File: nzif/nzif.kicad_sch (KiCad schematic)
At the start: 14 parts, among them J1 Rx, J10 ADAU1467_GPIOS, J11 ADAU1467_AUX_ADCS, J4 6V, J6 Microcontroller, J7 USBi, J8 I2S2, J9 I2S1

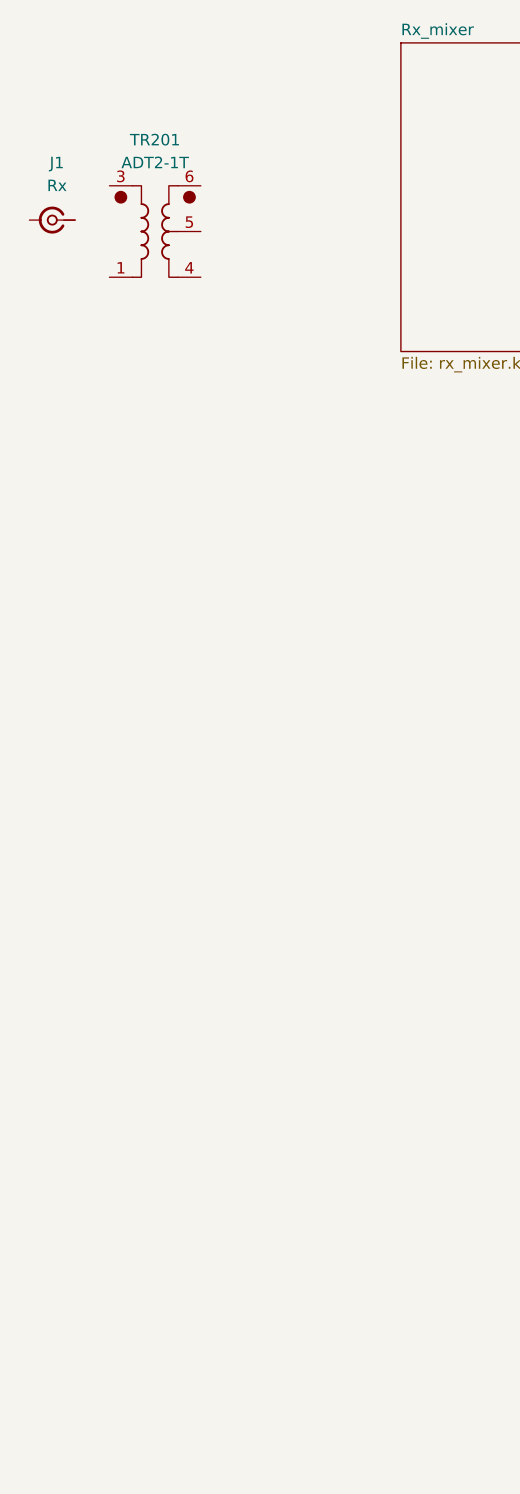
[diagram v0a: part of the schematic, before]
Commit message: changed to 1:1 transformer
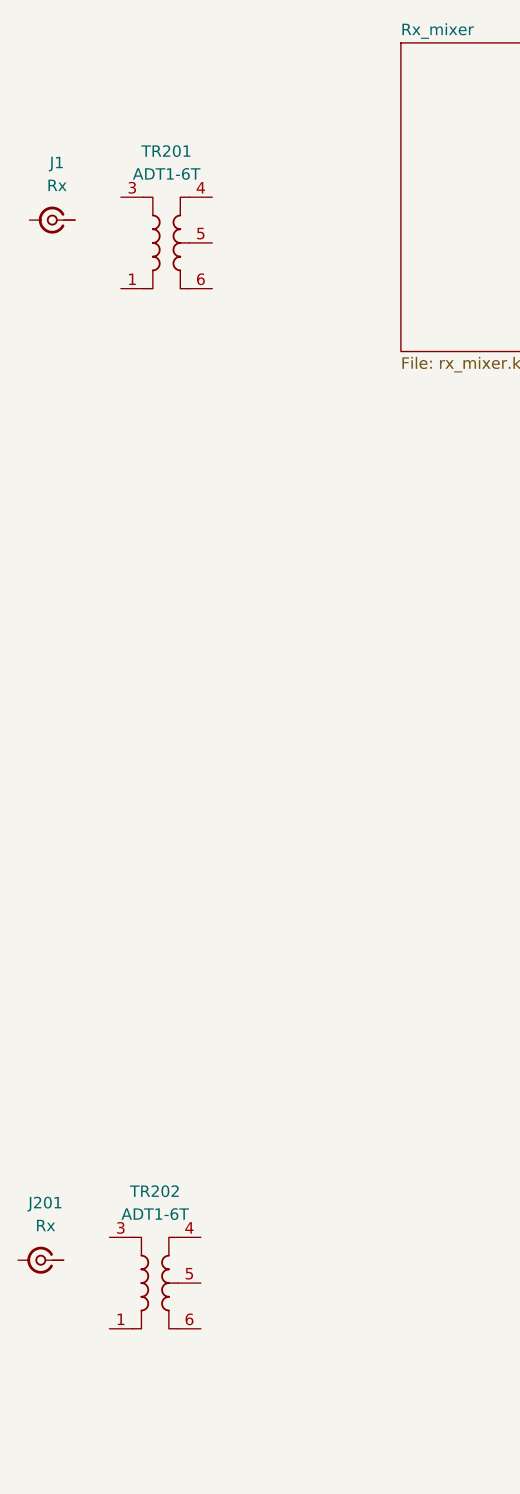
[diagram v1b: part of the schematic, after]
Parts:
- removed TR201: ADT2-1T, RF_Mini-Circuits:Mini-Circuits_CD542_H2.84mm, symbol Transformer:ADT2-1T
- added J201: Rx, symbol Connector:Conn_Coaxial_Small
- added TR201, TR202: ADT1-6T, RF_Mini-Circuits:Mini-Circuits_CD637_H5.23mm, symbol Transformer:ADT1-6T
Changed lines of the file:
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@@
-	)
-	(symbol
-		(lib_id "Transformer:ADT2-1T")
-		(at 41.91 38.1 0)
-		(unit 1)
-		(exclude_from_sim no)
-		(in_bom yes)
-		(on_board yes)
-		(dnp no)
-		(fields_autoplaced yes)
-		(property "Reference" "TR201"
-			(at 41.91 27.94 0)
-			(effects
-				(font
-					(size 1.27 1.27)
-				)
-			)
-		)
-		(property "Value" "ADT2-1T"
-			(at 41.91 30.48 0)
-			(effects
-				(font
-					(size 1.27 1.27)
-				)
-			)
-		)
-		(property "Footprint" "RF_Mini-Circuits:Mini-Circuits_CD542_H2.84mm"
-			(at 41.91 46.99 0)
-			(effects
-				(font
-					(size 1.27 1.27)
-				)
-				(hide yes)
-			)
-		)
-		(property "Datasheet" "https://www.minicircuits.com/pdfs/ADT2-1T+.pdf"
-			(at 41.91 38.1 0)
-			(effects
-				(font
-					(size 1.27 1.27)
-				)
-				(hide yes)
-			)
-		)
-		(property "Description" "0.40-450MHz 1:2 RF Transformer, Unbalanced to Balanced Center Tap, CD542"
-			(at 41.91 38.1 0)
-			(effects
-				(font
-					(size 1.27 1.27)
-				)
-				(hide yes)
-			)
-		)
-		(pin "2"
-		)
-		(pin "6"
-		)
-		(pin "5"
-		)
-		(pin "4"
-		)
-		(pin "3"
-		)
-		(pin "1"
-		)
-		(instances
-			(project ""
-				(path "/fe42ca2f-2bb8-4d5a-9e84-807788ed632f"
-					(reference "TR201")
-					(unit 1)
-				)
-			)
-		)
 	)
 	(symbol
@@
 	)
 	(symbol
+		(lib_id "Transformer:ADT1-6T")
+		(at 41.91 154.94 0)
+		(unit 1)
+		(exclude_from_sim no)
+		(in_bom yes)
+		(on_board yes)
+		(dnp no)
+		(fields_autoplaced yes)
+		(property "Reference" "TR202"
+			(at 41.91 144.78 0)
+			(effects
+				(font
+					(size 1.27 1.27)
+				)
+			)
+		)
+		(property "Value" "ADT1-6T"
+			(at 41.91 147.32 0)
+			(effects
+				(font
+					(size 1.27 1.27)
+				)
+			)
+		)
+		(property "Footprint" "RF_Mini-Circuits:Mini-Circuits_CD637_H5.23mm"
+			(at 41.91 163.83 0)
+			(effects
+				(font
+					(size 1.27 1.27)
+				)
+				(hide yes)
+			)
+		)
+		(property "Datasheet" "https://www.minicircuits.com/pdfs/ADT1-6T+.pdf"
+			(at 41.91 154.94 0)
+			(effects
+				(font
+					(size 1.27 1.27)
+				)
+				(hide yes)
+			)
+		)
+		(property "Description" "0.06-160MHz 1:1 RF Transformer, Unbalanced to Balanced Center Tap, CD542"
+			(at 41.91 154.94 0)
+			(effects
+				(font
+					(size 1.27 1.27)
+				)
+				(hide yes)
+			)
+		)
+		(pin "1"
+		)
+		(pin "5"
+		)
+		(pin "4"
+		)
+		(pin "6"
+		)
+		(pin "3"
+		)
+		(instances
+			(project "nzif"
+				(path "/fe42ca2f-2bb8-4d5a-9e84-807788ed632f"
+					(reference "TR202")
+					(unit 1)
+				)
+			)
+		)
+	)
+	(symbol
 		(lib_id "Device:R_Small_US")
 		(at 398.78 45.72 270)
@@
 	)
 	(symbol
+		(lib_id "Transformer:ADT1-6T")
+		(at 43.18 39.37 0)
+		(unit 1)
+		(exclude_from_sim no)
+		(in_bom yes)
+		(on_board yes)
+		(dnp no)
+		(fields_autoplaced yes)
+		(property "Reference" "TR201"
+			(at 43.18 29.21 0)
+			(effects
+				(font
+					(size 1.27 1.27)
+				)
+			)
+		)
+		(property "Value" "ADT1-6T"
+			(at 43.18 31.75 0)
+			(effects
+				(font
+					(size 1.27 1.27)
+				)
+			)
+		)
+		(property "Footprint" "RF_Mini-Circuits:Mini-Circuits_CD637_H5.23mm"
+			(at 43.18 48.26 0)
+			(effects
+				(font
+					(size 1.27 1.27)
+				)
+				(hide yes)
+			)
+		)
+		(property "Datasheet" "https://www.minicircuits.com/pdfs/ADT1-6T+.pdf"
+			(at 43.18 39.37 0)
+			(effects
+				(font
+					(size 1.27 1.27)
+				)
+				(hide yes)
+			)
+		)
+		(property "Description" "0.06-160MHz 1:1 RF Transformer, Unbalanced to Balanced Center Tap, CD542"
+			(at 43.18 39.37 0)
+			(effects
+				(font
+					(size 1.27 1.27)
+				)
+				(hide yes)
+			)
+		)
+		(pin "1"
+		)
+		(pin "5"
+		)
+		(pin "4"
+		)
+		(pin "6"
+		)
+		(pin "3"
+		)
+		(instances
+			(project ""
+				(path "/fe42ca2f-2bb8-4d5a-9e84-807788ed632f"
+					(reference "TR201")
+					(unit 1)
+				)
+			)
+		)
+	)
+	(symbol
 		(lib_id "Connector_Generic:Conn_02x10_Odd_Even")
 		(at 346.71 78.74 0)
@@
 					(unit 1)
 				)
+			)
+		)
+	)
+	(symbol
+		(lib_id "Connector:Conn_Coaxial_Small")
+		(at 29.21 152.4 180)
+		(unit 1)
+		(exclude_from_sim no)
+		(in_bom yes)
+		(on_board yes)
+		(dnp no)
+		(fields_autoplaced yes)
+		(property "Reference" "J201"
+			(at 29.7295 146.05 0)
+			(effects
+				(font
+					(size 1.27 1.27)
+				)
+			)
+		)
+		(property "Value" "Rx"
+			(at 29.7295 148.59 0)
+			(effects
+				(font
+					(size 1.27 1.27)
+				)
+			)
+		)
+		(property "Footprint" ""
+			(at 29.21 152.4 0)
+			(effects
+				(font
+					(size 1.27 1.27)
+				)
+				(hide yes)
+			)
+		)
+		(property "Datasheet" "~"
+			(at 29.21 152.4 0)
+			(effects
+				(font
+					(size 1.27 1.27)
+				)
+				(hide yes)
+			)
+		)
+		(property "Description" "small coaxial connector (BNC, SMA, SMB, SMC, Cinch/RCA, LEMO, ...)"
+			(at 29.21 152.4 0)
+			(effects
+				(font
+					(size 1.27 1.27)
+				)
+				(hide yes)
+			)
+		)
+		(pin "2"
+		)
+		(pin "1"
+		)
+		(instances
+			(project "nzif"
+				(path "/fe42ca2f-2bb8-4d5a-9e84-807788ed632f"
+					(reference "J201")
+					(unit 1)
+				)

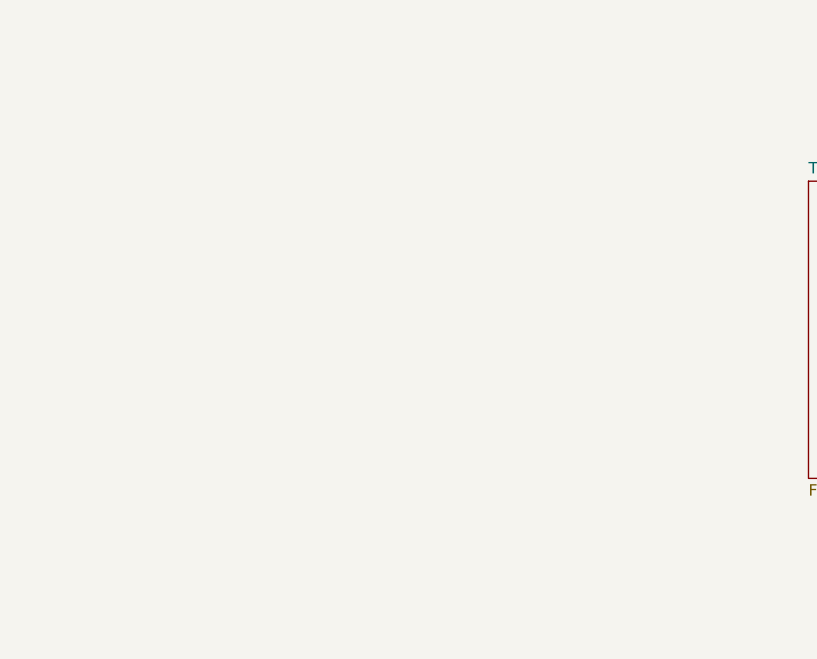
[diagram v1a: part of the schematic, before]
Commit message: added Tx Mixer
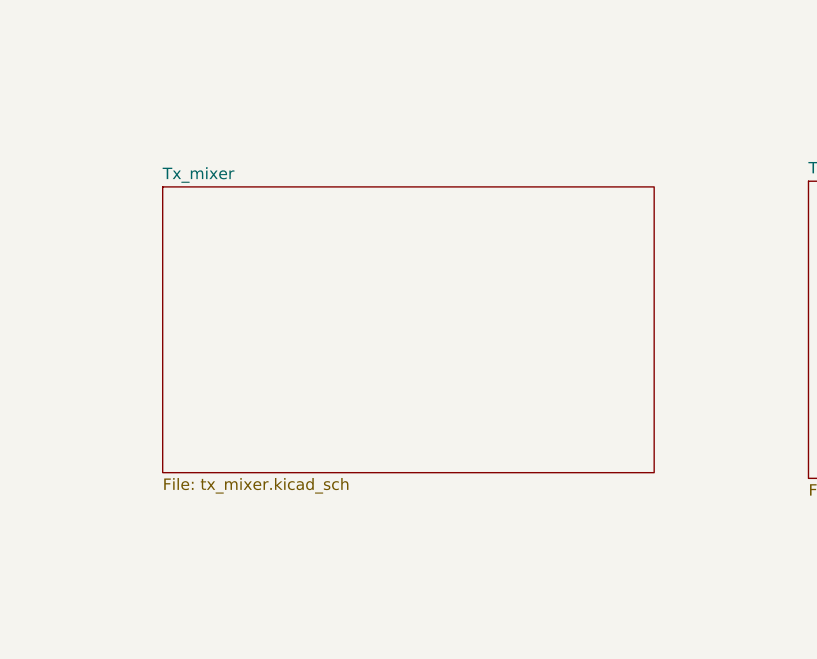
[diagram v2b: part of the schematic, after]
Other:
- added sheet Tx_mixer (tx_mixer.kicad_sch)
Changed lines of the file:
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@@
+	)
+	(sheet
+		(at 66.04 137.16)
+		(size 54.61 31.75)
+		(exclude_from_sim no)
+		(in_bom yes)
+		(on_board yes)
+		(dnp no)
+		(fields_autoplaced yes)
+		(stroke
+			(width 0.1524)
+			(type solid)
+		)
+		(fill
+			(color 0 0 0 0.0000)
+		)
+		(property "Sheetname" "Tx_mixer"
+			(at 66.04 136.4484 0)
+			(effects
+				(font
+					(size 1.27 1.27)
+				)
+				(justify left bottom)
+			)
+		)
+		(property "Sheetfile" "tx_mixer.kicad_sch"
+			(at 66.04 169.4946 0)
+			(effects
+				(font
+					(size 1.27 1.27)
+				)
+				(justify left top)
+			)
+		)
+		(instances
+			(project "nzif"
+				(path "/fe42ca2f-2bb8-4d5a-9e84-807788ed632f"
+					(page "13")
+				)
+			)
+		)
 	)
 	(sheet

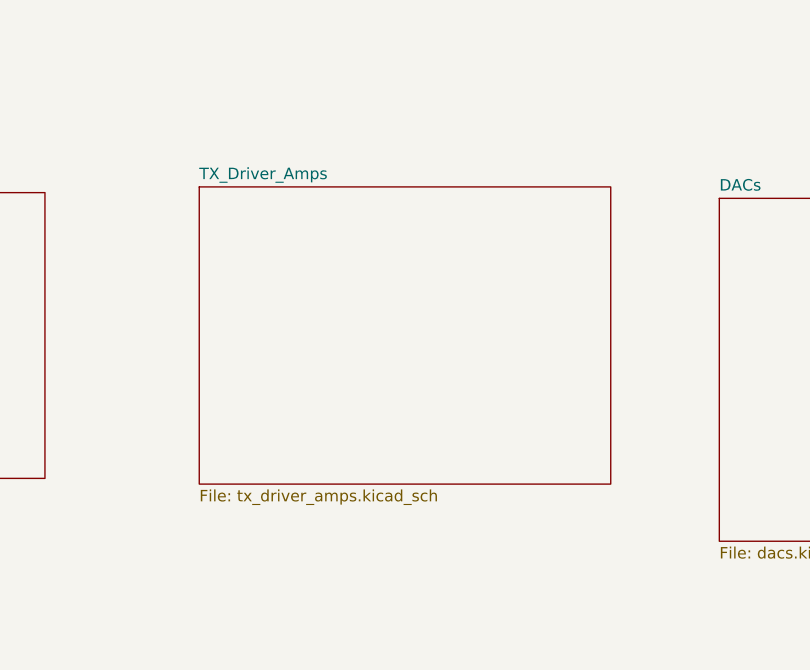
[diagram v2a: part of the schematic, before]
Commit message: removed unnecessary Tx driver amp sheet
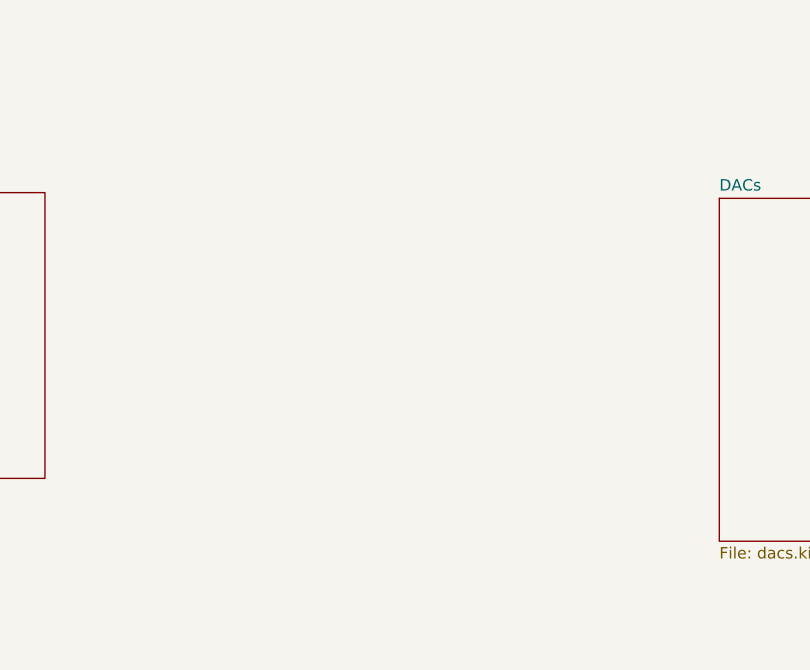
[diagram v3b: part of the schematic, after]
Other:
- removed sheet TX_Driver_Amps
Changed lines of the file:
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@@
-	)
-	(sheet
-		(at 137.795 136.525)
-		(size 45.72 33.02)
-		(exclude_from_sim no)
-		(in_bom yes)
-		(on_board yes)
-		(dnp no)
-		(fields_autoplaced yes)
-		(stroke
-			(width 0.1524)
-			(type solid)
-		)
-		(fill
-			(color 0 0 0 0.0000)
-		)
-		(property "Sheetname" "TX_Driver_Amps"
-			(at 137.795 135.8134 0)
-			(effects
-				(font
-					(size 1.27 1.27)
-				)
-				(justify left bottom)
-			)
-		)
-		(property "Sheetfile" "tx_driver_amps.kicad_sch"
-			(at 137.795 170.1296 0)
-			(effects
-				(font
-					(size 1.27 1.27)
-				)
-				(justify left top)
-			)
-		)
-		(instances
-			(project "nzif"
-				(path "/fe42ca2f-2bb8-4d5a-9e84-807788ed632f"
-					(page "12")
-				)
-			)
-		)
 	)
 	(sheet

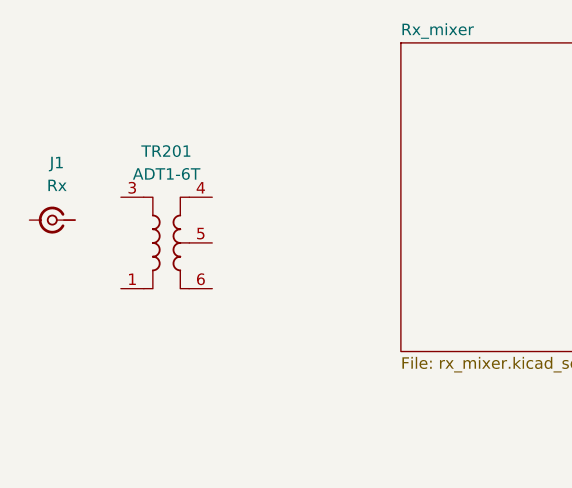
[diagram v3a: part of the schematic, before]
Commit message: changed Rx mixer from 8 phase to classic tayloe
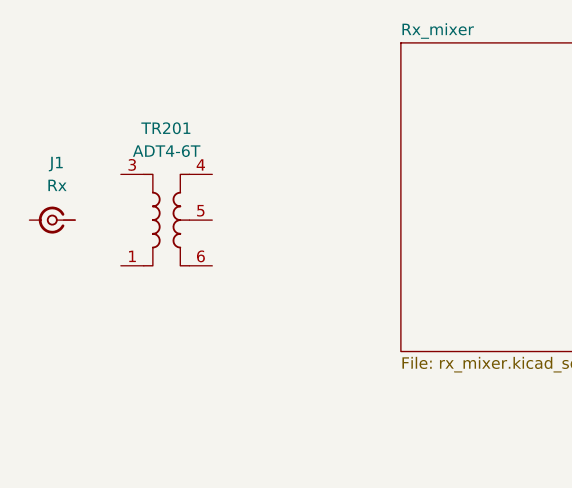
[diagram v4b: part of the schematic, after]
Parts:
- removed TR201: ADT1-6T, RF_Mini-Circuits:Mini-Circuits_CD637_H5.23mm, symbol Transformer:ADT1-6T
- added TR201: ADT4-6T, RF_Mini-Circuits:Mini-Circuits_CD637_H5.23mm, symbol Transformer:ADT4-6T
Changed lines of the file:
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@@
-	)
-	(symbol
-		(lib_id "Transformer:ADT1-6T")
-		(at 43.18 39.37 0)
-		(unit 1)
-		(exclude_from_sim no)
-		(in_bom yes)
-		(on_board yes)
-		(dnp no)
-		(fields_autoplaced yes)
-		(property "Reference" "TR201"
-			(at 43.18 29.21 0)
-			(effects
-				(font
-					(size 1.27 1.27)
-				)
-			)
-		)
-		(property "Value" "ADT1-6T"
-			(at 43.18 31.75 0)
-			(effects
-				(font
-					(size 1.27 1.27)
-				)
-			)
-		)
-		(property "Footprint" "RF_Mini-Circuits:Mini-Circuits_CD637_H5.23mm"
-			(at 43.18 48.26 0)
-			(effects
-				(font
-					(size 1.27 1.27)
-				)
-				(hide yes)
-			)
-		)
-		(property "Datasheet" "https://www.minicircuits.com/pdfs/ADT1-6T+.pdf"
-			(at 43.18 39.37 0)
-			(effects
-				(font
-					(size 1.27 1.27)
-				)
-				(hide yes)
-			)
-		)
-		(property "Description" "0.06-160MHz 1:1 RF Transformer, Unbalanced to Balanced Center Tap, CD542"
-			(at 43.18 39.37 0)
-			(effects
-				(font
-					(size 1.27 1.27)
-				)
-				(hide yes)
-			)
-		)
-		(pin "1"
-		)
-		(pin "5"
-		)
-		(pin "4"
-		)
-		(pin "6"
-		)
-		(pin "3"
-		)
-		(instances
-			(project ""
-				(path "/fe42ca2f-2bb8-4d5a-9e84-807788ed632f"
-					(reference "TR201")
-					(unit 1)
-				)
-			)
-		)
 	)
 	(symbol
@@
 					(unit 1)
 				)
+			)
+		)
+	)
+	(symbol
+		(lib_id "Transformer:ADT4-6T")
+		(at 43.18 36.83 0)
+		(unit 1)
+		(exclude_from_sim no)
+		(in_bom yes)
+		(on_board yes)
+		(dnp no)
+		(fields_autoplaced yes)
+		(property "Reference" "TR201"
+			(at 43.18 26.67 0)
+			(effects
+				(font
+					(size 1.27 1.27)
+				)
+			)
+		)
+		(property "Value" "ADT4-6T"
+			(at 43.18 29.21 0)
+			(effects
+				(font
+					(size 1.27 1.27)
+				)
+			)
+		)
+		(property "Footprint" "RF_Mini-Circuits:Mini-Circuits_CD637_H5.23mm"
+			(at 43.18 45.72 0)
+			(effects
+				(font
+					(size 1.27 1.27)
+				)
+				(hide yes)
+			)
+		)
+		(property "Datasheet" "https://www.minicircuits.com/pdfs/ADT4-6T+.pdf"
+			(at 43.18 36.83 0)
+			(effects
+				(font
+					(size 1.27 1.27)
+				)
+				(hide yes)
+			)
+		)
+		(property "Description" "1.5-70MHz 1:4 RF Transformer, Unbalanced to Balanced Center Tap, CD637"
+			(at 43.18 36.83 0)
+			(effects
+				(font
+					(size 1.27 1.27)
+				)
+				(hide yes)
+			)
+		)
+		(pin "3"
+		)
+		(pin "4"
+		)
+		(pin "6"
+		)
+		(pin "1"
+		)
+		(pin "5"
+		)
+		(instances
+			(project ""
+				(path "/fe42ca2f-2bb8-4d5a-9e84-807788ed632f"
+					(reference "TR201")
+					(unit 1)
+				)
